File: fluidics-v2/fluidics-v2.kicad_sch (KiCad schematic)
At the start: 38 parts, among them J1 PJ-063AH, J10 87832-1010, J11 0705430001, J12 87832-1010, J13 0705430001, J14 87832-1010, J15 0533980671, J16 0705430001, J17 0533980671, J18 87832-1010, J19 0705430001, J2 B6B-ZR-SM4-TF, J20 0533980671, J21 87832-1010, J22 0705430001, J23 0533980671, J3 A-DS_15_A_KG-T4S, J4 B6B-ZR-SM4-TF, J5 1860280, J6 Conn_02x14_Counter_Clockwise, J7 Conn_02x03_Odd_Even, J8 705430039, J9 522712079, U2 Teensy4.1

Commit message: V3: strip to minimal fluidics config, add 6th selector valve, fix lib paths
Reduce the V2 fluidics controller to a minimal build and extend the
selector-valve bank:

- Remove disc-pump driver (U1, M1); keep the syringe pump only
- Remove the solenoid-valve subsystem (MCZ33996 IC1 + D5-D20 + R6-R21
  + connector J5) -- 16 solenoids -> 0
- Remove all SPI pressure sensors (IC3-IC6 and their passives) -- 4 -> 0
- Reduce I2C flow sensors 4 -> 3 (drop connector J17)
- Add a 6th IDEX selector-valve channel (connectors J24/J25) on the
  shared isolated-I2C + 24V bus
- Remove the Wenzel-lab pressure-controller daughter board interface
  (J6, J7/ICSP, J8, JP3)
- Remove the manual-control block (switches S1-S4, push-button SW1,
  potentiometer VR1, TCA9539 U7, pull-ups, jumpers)
- Remove the 24V->12V converter (U5 + indicator D1/R2 + power-good R52);
  no remaining 12V load after the above

Net component count: 177 -> 86 footprints. DRC: 0 unconnected.

Tooling/portability fixes:
- Rewrite fp-lib-table and sym-lib-table: replace the original author's
  hardcoded absolute paths (/home/octopi-codex/...) with ${KIPRJMOD}-
  relative URIs so the libraries resolve on any machine
- Migrate the project to KiCad 10 format
- Add .gitignore for KiCad lock/autosave/cache and editor history files
- Add fluidics-v3-schematic.pdf (rendered schematic for review)

Co-Authored-By: Claude Opus 4.8 (1M context) <noreply@anthropic.com>
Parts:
- removed J17: 0533980671, molex_connectors:MOLEX_0533980671, symbol 0533980671:0533980671
- removed J5: 1860280, phoenix_2:1860280, symbol 1860280:1860280
- removed J6: Conn_02x14_Counter_Clockwise, Package_DIP:DIP-28_W15.24mm_Socket, symbol Connector_Generic:Conn_02x14_Counter_Clockwise
- removed J7: Conn_02x03_Odd_Even, Connector_PinHeader_2.54mm:PinHeader_2x03_P2.54mm_Vertical, symbol Connector_Generic:Conn_02x03_Odd_Even
- removed J8: 705430039, 70543-0039_MOL, symbol 0705430004:705430039
- removed JP3: SolderJumper_2_Bridged, Jumper:SolderJumper-2_P1.3mm_Bridged_Pad1.0x1.5mm, symbol Jumper:SolderJumper_2_Bridged
- removed M1: ~, TTP Ventus:Pump Mount, symbol ttp:Pump_Mounting
- removed R1: 0, Resistor_SMD:R_0603_1608Metric, symbol Device:R
- removed R54: 4.7k, Resistor_SMD:R_0402_1005Metric, symbol Device:R
- removed U1: ~, TTP Ventus:Disc_Pump_Driver_PCB, symbol ttp:59017-200-0003
- added J24: 0705430001, molex_connectors:SHDR2W64P0X254_1X2_737X660X1181P, symbol 0705430001:0705430001
- added J25: 87832-1010, molex_connectors:878321010, symbol 87832-1010:87832-1010
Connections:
- net +24V: now also J24.2
- net GND: now also J24.1, J25.4
- net Selector Valves/SCL 5V: now also J25.2
- net Selector Valves/SDA 5V: now also J25.1
- no-connect marks 108 -> 85
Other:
- removed sheet Solenoid Valves
- note removed: "Connect up to 16 solenoid valves"
- note removed: "Connections for powering the daughter board"
- note removed: "Disc pump module"
- note removed: "ICSP"
- note removed: "Mounting holes for the pump"
- note removed: "Note: Cut the jumper when using the ICSP header and bridge it when done. Pressure controller module from Wenzel lab"
- moved on the sheet: J10, J11, J12, J13, J14, J16, J18, J19, J21, J22, TP1, TP2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

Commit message: @ WIP: continue strip-down — empty sensors sheet, drop 11 PCB footprints
Recovered in-progress work from the previous KiCad session (restored via
KiCad session recovery). This is mid-edit, not a finished config:
- sensors.kicad_sch: 17 -> 0 symbols (sheet fully emptied)
- fluidics-v2.kicad_pcb: 86 -> 75 footprints
- fluidics-v2.kicad_sch: minor net/sheet cleanup

Schematic + libraries validated with kicad-cli sch export netlist (exit 0).

Co-Authored-By: Claude Opus 4.8 (1M context) <noreply@anthropic.com>
@
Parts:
- renumbered J23 to J17
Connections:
- net SCL2: now also J17.2
- net SDA2: now also J17.5
- net Sensors/SCL_OUT: no longer J17.2
- net Sensors/SDA_OUT: no longer J17.5
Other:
- note added: "Four air pressure sensors, three flow sensors (V3)"
- note removed: "Four air pressure sensors, four flow sensors"
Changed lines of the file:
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@@
 		)
 	)
-	(text "Four air pressure sensors, \nfour flow sensors"
+	(text "Four air pressure sensors, \nthree flow sensors (V3)"
 		(exclude_from_sim no)
 		(at 326.39 201.93 0)
@@
 	(wire
 		(pts
-			(xy 375.92 203.2) (xy 388.62 203.2)
-		)
-		(stroke
-			(width 0)
-			(type default)
-		)
-	)
-	(wire
-		(pts
 			(xy 309.88 186.69) (xy 317.5 186.69)
 		)
@@
 		)
 	)
-	(wire
-		(pts
-			(xy 375.92 205.74) (xy 396.24 205.74)
-		)
-		(stroke
-			(width 0)
-			(type default)
-		)
-	)
 	(bus
 		(pts
@@
 	(wire
 		(pts
-			(xy 396.24 205.74) (xy 396.24 228.6)
-		)
-		(stroke
-			(width 0)
-			(type default)
-		)
-	)
-	(wire
-		(pts
-			(xy 388.62 203.2) (xy 388.62 228.6)
-		)
-		(stroke
-			(width 0)
-			(type default)
-		)
-	)
-	(wire
-		(pts
 			(xy 160.02 115.57) (xy 160.02 116.84)
 		)
@@
 		)
 	)
+	(label "SDA2"
+		(at 396.24 228.6 90)
+		(effects
+			(font
+				(size 1.27 1.27)
+			)
+			(justify left bottom)
+		)
+	)
 	(label "SCL2"
 		(at 219.71 231.14 0)
@@
 		)
 	)
+	(label "SCL2"
+		(at 388.62 228.6 90)
+		(effects
+			(font
+				(size 1.27 1.27)
+			)
+			(justify left bottom)
+		)
+	)
 	(label "GPIO_2"
 		(at 284.48 203.2 0)
@@
 		(in_pos_files yes)
 		(dnp no)
-		(property "Reference" "J23"
+		(property "Reference" "J17"
 			(at 406.4 245.11 90)
 			(show_name no)
@@
 			(project "fluidics-v2"
 				(path "/0ec91c42-8aad-437d-8c85-5e10f0e51fe0"
-					(reference "J23")
+					(reference "J17")
 					(unit 1)
 				)

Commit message: @ Remove J9 daughterboard connector; restore Back GND plane; fix thermals
- Delete J9 (20-pin FPC to motor-control daughterboard) from PCB + schematic;
  its SPI/GPIO went nowhere else on-board (75 -> 74 footprints)
- Remove orphaned GPIO_1-9 / SPI_MOSI / SPI_MISO copper (72 tracks, 11 vias)
  plus the ex-J9 dangling stub vias on the I2C/SCK buses
- Reassign the floating no-net Back pour to GND: clears isolated_copper and
  restores a continuous back-side ground plane
- Set U4/J15/D2 GND pads to solid zone connection: clears starved_thermal
- DRC: 229 -> 217 violations. starved_thermal 3->0, isolated_copper 1->0,
  via_dangling 7->0. Remaining ~217 are cosmetic silk/courtyard/library
  warnings inherited from upstream.

Co-Authored-By: Claude Opus 4.8 (1M context) <noreply@anthropic.com>
@
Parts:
- removed J9: 522712079, 0522712079:CON_522712079_MOL, symbol 0522712079:522712079
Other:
- note removed: "Connection to daughter board I2C 0 - I2C 2 (6 wires) 3.3V 5V 12V 24V SPI (3 wires) GPIO (10 wires)"
- note removed: "These connectors are optional"

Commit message: @ Wire solenoid driver + status LEDs + I2C cleanup; route + connect
- Solenoid driver (U1 TPL7407): IN1-7 <- Teensy GPIO_1-7 (back-layer fanout,
  vias off the SMD pads), COM->+24V, GND->plane, OUT1-7 -> J5 screw terminal
- Add 7 solenoid status LEDs (GPIO_1-7) + COM/+24V indicator LED (0402)
- Remove LTC4311 I2C accelerators (U9/U10) - misbehaved on lightly-loaded
  buses (single-valve failure); kept passive pull-ups. Restored SCL2/SDA2
  pull-ups (R41/R42)
- Back layer: full-board GND pour (clean rectangle outline)
- Connect U1 GND and R4 (+24V power-indicator LED) to their nets

DRC: unconnected down to 5, all intentional unused-pin no-connects
(GPIO_8/9 + vestigial SPI). No shorts; vias cleared out of Teensy SMD pads.

Co-Authored-By: Claude Opus 4.8 (1M context) <noreply@anthropic.com>
@
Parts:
- removed R53: 4.7k, Resistor_SMD:R_0402_1005Metric, symbol Device:R
- added D1, D10, D11, D5, D6, D7, D8, D9: LED, LED_SMD:LED_0402_1005Metric, symbol Device:LED
- added R1, R11, R2, R6, R7, R8, R9: 2.7K, Resistor_SMD:R_0402_1005Metric, symbol Device:R
- added R10: 42K, Resistor_SMD:R_0603_1608Metric, symbol Device:R
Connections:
- net +24V: now also R10.1
- net GND: now also D1.1 (K), D10.1 (K), D11.1 (K), D5.1 (K), D6.1 (K), D7.1 (K), D8.1 (K), D9.1 (K)
- net GPIO_1: now also R1.1
- net GPIO_2: now also R2.1
- net GPIO_3: now also R6.1
- net GPIO_4: now also R7.1
- net GPIO_5: now also R8.1
- net GPIO_6: now also R9.1
- net GPIO_7: now also R11.1
- new net: D7.2 (A), R7.2
- new net: D5.2 (A), R2.2
- new net: D6.2 (A), R6.2
- new net: D9.2 (A), R9.2
- new net: D10.2 (A), R10.2
- new net: D8.2 (A), R8.2
- new net: D1.2 (A), R1.2
- new net: D11.2 (A), R11.2
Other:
- added sheet Solenoid Valve Driver (solenoid_driver.kicad_sch)
- note added: "Indicator LEDs for +24V Solenoid Driver and 7 Driver Inputs"
- moved on the sheet: J10, J11, J12, J13, J14, J16, J18, J19, J21, J22, J24, J25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

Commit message: Trim board: remove D1/D5-D8/R1/R2/R6-R8/H1, add connector J6
PCB + root schematic + solenoid_driver sheet edits (GUI-driven).
Footprints 85 -> 75. Removed diodes D1/D5-D8, resistors R1/R2/R6-R8,
mounting hole H1; added connector J6. Schematic/PCB in parity
(kicad-cli drc: schematic_parity 0). Remaining DRC items are the
inherited-from-upstream cosmetic set (silk_over_copper, malformed
_courtyard, lib_footprint_mismatch) plus 5 intentional no-connects
and 1 dangling track.

Co-Authored-By: Claude Opus 4.8 (1M context) <noreply@anthropic.com>
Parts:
- removed D1, D5, D6, D7, D8: LED, LED_SMD:LED_0402_1005Metric, symbol Device:LED
- removed H1: MountingHole_Pad, MountingHole:MountingHole_3.2mm_M3_Pad_Via, symbol Mechanical:MountingHole_Pad
- removed R1, R2, R6, R7, R8: 2.7K, Resistor_SMD:R_0402_1005Metric, symbol Device:R
- H2, H3, H4: footprint MountingHole:MountingHole_3.2mm_M3_Pad_Via -> MountingHole:MountingHole_2.2mm_M2_Pad_Via
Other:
- moved on the sheet: D10, D11, D9, R10, R11, R9

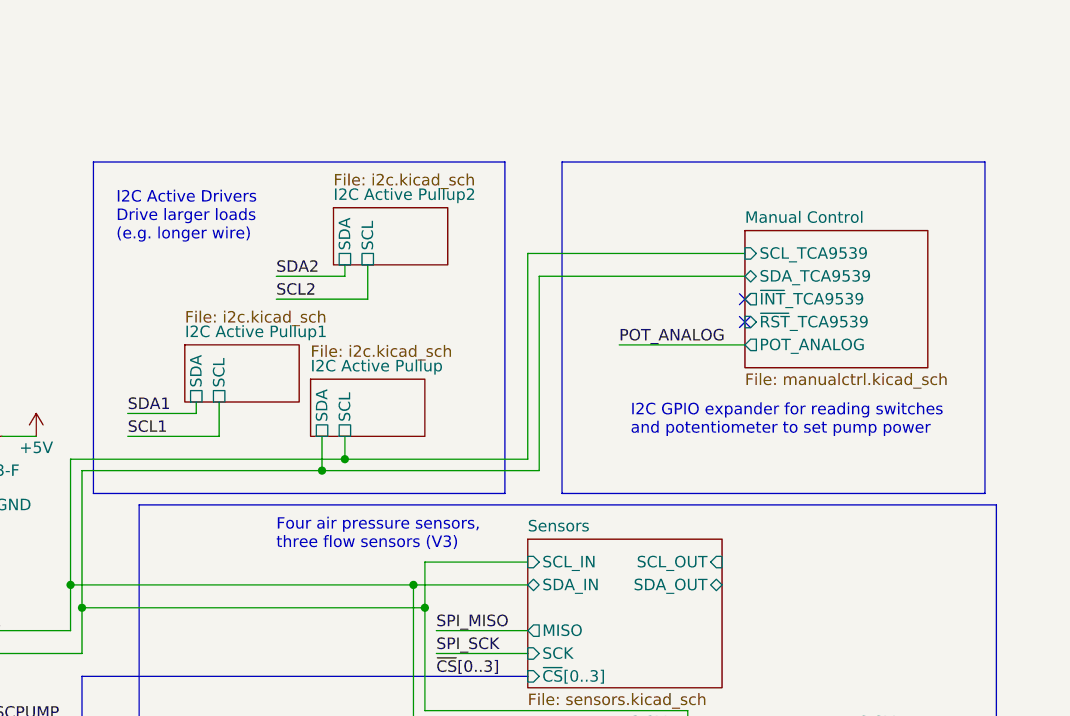
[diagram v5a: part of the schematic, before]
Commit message: Place Cephla logo on F.SilkS (30%), add logo footprints; i2c sheet edit
- Placed bitmap2component logo (ref G***) on front silkscreen, scaled
  to 30% of original -> 12.40 x 4.88 mm; footprints 75 -> 76.
- Add logo source footprints: ImageCephlaCompanyPCB.kicad_mod (full)
  + _30pct (placed variant). Abandoned Attempt2/3 left untracked.
- i2c.kicad_sch: non-component edit (wiring/label), saved from GUI.

Co-Authored-By: Claude Opus 4.8 (1M context) <noreply@anthropic.com>
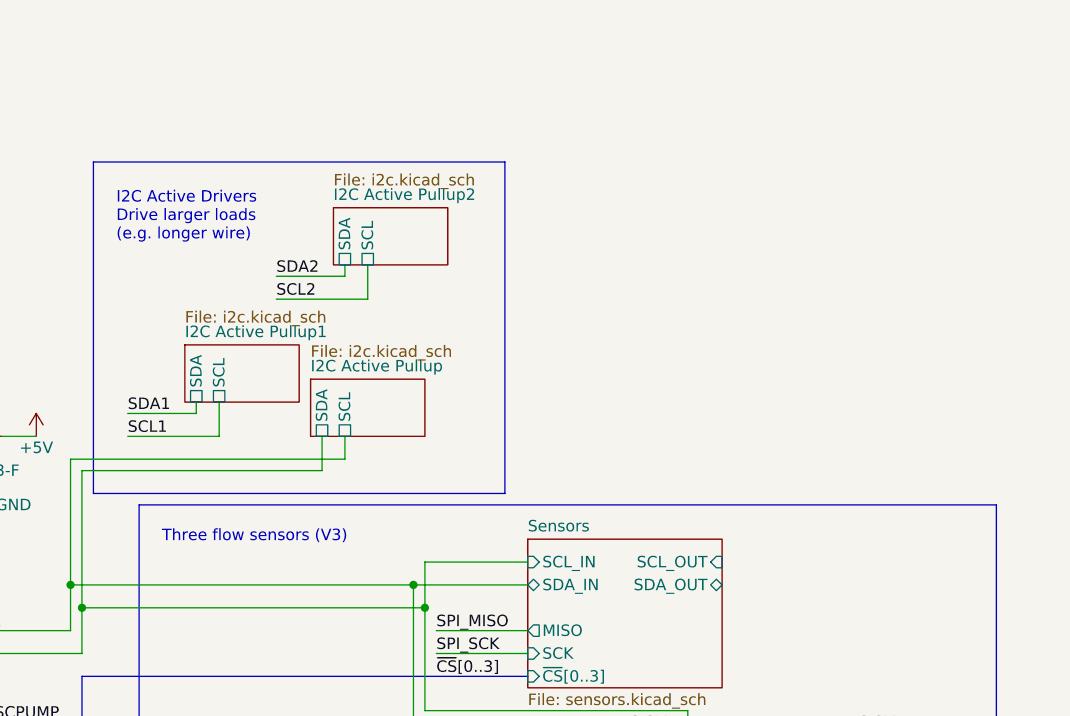
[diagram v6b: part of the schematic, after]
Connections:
- no-connect marks 85 -> 83
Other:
- removed sheet Manual Control
- note added: "Three flow sensors (V3)"
- note removed: "Four air pressure sensors, three flow sensors (V3)"
- note removed: "I2C GPIO expander for reading switches and potentiometer to set pump power"
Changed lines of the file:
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@@
 	)
 	(rectangle
-		(start 358.14 158.75)
-		(end 405.13 195.58)
-		(stroke
-			(width 0)
-			(type default)
-		)
-		(fill
-			(type none)
-		)
-	)
-	(rectangle
 		(start 203.2 130.81)
 		(end 265.43 171.45)
@@
 		)
 	)
-	(text "Four air pressure sensors, \nthree flow sensors (V3)"
+	(text "Three flow sensors (V3)"
 		(exclude_from_sim no)
-		(at 326.39 201.93 0)
+		(at 313.69 201.168 0)
 		(effects
 			(font
@@
 		)
 	)
-	(text "I2C GPIO expander for reading switches \nand potentiometer to set pump power"
-		(exclude_from_sim no)
-		(at 365.76 189.23 0)
-		(effects
-			(font
-				(size 1.27 1.27)
-			)
-			(justify left bottom)
-		)
-	)
 	(text "Selector valve power"
 		(exclude_from_sim no)
@@
 	)
 	(junction
-		(at 334.01 191.77)
-		(diameter 0)
-		(color 0 0 0 0)
-	)
-	(junction
 		(at 227.33 120.65)
 		(diameter 0)
@@
 	)
 	(junction
-		(at 331.47 193.04)
-		(diameter 0)
-		(color 0 0 0 0)
-	)
-	(junction
 		(at 327.66 104.14)
 		(diameter 0)
@@
 	)
 	(no_connect
-		(at 378.46 176.53)
-	)
-	(no_connect
 		(at 313.69 228.6)
 	)
@@
 	)
 	(no_connect
-		(at 378.46 173.99)
-	)
-	(no_connect
 		(at 175.26 146.05)
 	)
@@
 	(wire
 		(pts
-			(xy 331.47 193.04) (xy 355.6 193.04)
-		)
-		(stroke
-			(width 0)
-			(type default)
-		)
-	)
-	(wire
-		(pts
 			(xy 257.81 114.3) (xy 261.62 114.3)
 		)
@@
 	(wire
 		(pts
-			(xy 355.6 193.04) (xy 355.6 171.45)
-		)
-		(stroke
-			(width 0)
-			(type default)
-		)
-	)
-	(wire
-		(pts
 			(xy 182.88 163.83) (xy 157.48 163.83)
 		)
@@
 	(wire
 		(pts
-			(xy 354.33 168.91) (xy 378.46 168.91)
-		)
-		(stroke
-			(width 0)
-			(type default)
-		)
-	)
-	(wire
-		(pts
 			(xy 284.48 248.92) (xy 302.26 248.92)
 		)
@@
 	(wire
 		(pts
-			(xy 334.01 191.77) (xy 354.33 191.77)
-		)
-		(stroke
-			(width 0)
-			(type default)
-		)
-	)
-	(wire
-		(pts
 			(xy 152.4 106.68) (xy 153.67 106.68)
 		)
@@
 	(wire
 		(pts
-			(xy 355.6 171.45) (xy 378.46 171.45)
-		)
-		(stroke
-			(width 0)
-			(type default)
-		)
-	)
-	(wire
-		(pts
 			(xy 135.89 275.59) (xy 156.21 275.59)
 		)
@@
 	(wire
 		(pts
-			(xy 354.33 168.91) (xy 354.33 191.77)
-		)
-		(stroke
-			(width 0)
-			(type default)
-		)
-	)
-	(wire
-		(pts
 			(xy 151.13 149.86) (xy 143.51 149.86)
 		)
@@
 	(wire
 		(pts
-			(xy 364.49 179.07) (xy 378.46 179.07)
-		)
-		(stroke
-			(width 0)
-			(type default)
-		)
-	)
-	(wire
-		(pts
 			(xy 193.04 184.15) (xy 193.04 248.92)
 		)
@@
 		)
 	)
-	(label "POT_ANALOG"
-		(at 364.49 179.07 0)
-		(effects
-			(font
-				(size 1.27 1.27)
-			)
-			(justify left bottom)
-		)
-	)
 	(label "~{CS}3"
 		(at 285.75 248.92 0)
@@
 				)
 			)
-		)
-	)
-	(sheet
-		(at 378.46 166.37)
-		(size 20.32 15.24)
-		(exclude_from_sim no)
-		(in_bom yes)
-		(on_board yes)
-		(dnp no)
-		(fields_autoplaced yes)
-		(stroke
-			(width 0.1524)
-			(type solid)
-		)
-		(fill
-			(color 0 0 0 0)
-		)
-		(property "Sheetname" "Manual Control"
-			(at 378.46 165.6584 0)
-			(show_name no)
-			(do_not_autoplace no)
-			(effects
-				(font
-					(size 1.27 1.27)
-				)
-				(justify left bottom)
-			)
-		)
-		(property "Sheetfile" "manualctrl.kicad_sch"
-			(at 378.46 182.1946 0)
-			(show_name no)
-			(do_not_autoplace no)
-			(effects
-				(font
-					(size 1.27 1.27)
-				)
-				(justify left top)
-			)
-		)
-		(pin "SCL_TCA9539" input
-			(at 378.46 168.91 180)
-			(effects
-				(font
-					(size 1.27 1.27)
-				)
-				(justify left)
-			)
-		)
-		(pin "SDA_TCA9539" bidirectional
-			(at 378.46 171.45 180)
-			(effects
-				(font
-					(size 1.27 1.27)
-				)
-				(justify left)
-			)
-		)
-		(pin "~{INT}_TCA9539" output
-			(at 378.46 173.99 180)
-			(effects
-				(font
-					(size 1.27 1.27)
-				)
-				(justify left)
-			)
-		)
-		(pin "POT_ANALOG" output
-			(at 378.46 179.07 180)
-			(effects
-				(font
-					(size 1.27 1.27)
-				)
-				(justify left)
-			)
-		)
-		(pin "~{RST}_TCA9539" input
-			(at 378.46 176.53 180)
-			(effects
-				(font
-					(size 1.27 1.27)
-				)
-				(justify left)
-			)
-		)
-		(instances
-			(project "fluidics-v2"
-				(path "/0ec91c42-8aad-437d-8c85-5e10f0e51fe0"
-					(page "5")
-				)
-			)
